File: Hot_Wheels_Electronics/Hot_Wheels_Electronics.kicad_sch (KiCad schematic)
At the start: 42 parts, among them J1 motor_output_a, J2 motor_output_b, J3 Conn_01x05_Socket, J4 Conn_01x02_Socket, J5 Conn_01x03_Socket, J6 Conn_01x06_Socket, J7 Conn_01x04_Socket, J8 Conn_01x02_Socket, M1 motor_driver: DRV8833PW, SW1 main_switch, U1 esp32-wemos-d1-mini, U2 ESP32-WROOM-32, U3 BMI160, U4 MiniBuck_3A, U5 MiniBuck_3A, U6 ADS1115IDGS

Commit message: separate motor connectors from battery family
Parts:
- J1, J2: footprint Connector_JST:JST_PH_S2B-PH-K_1x02_P2.00mm_Horizontal -> Connector_Molex:Molex_Micro-Fit_3.0_43650-0210_1x02-1MP_P3.00mm_Horizontal
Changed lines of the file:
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@@
 			)
 		)
-		(property "Footprint" "Connector_JST:JST_PH_S2B-PH-K_1x02_P2.00mm_Horizontal"
+		(property "Footprint" "Connector_Molex:Molex_Micro-Fit_3.0_43650-0210_1x02-1MP_P3.00mm_Horizontal"
 			(at 160.02 212.09 0)
 			(hide yes)
@@
 			)
 		)
-		(property "Footprint" "Connector_JST:JST_PH_S2B-PH-K_1x02_P2.00mm_Horizontal"
+		(property "Footprint" "Connector_Molex:Molex_Micro-Fit_3.0_43650-0210_1x02-1MP_P3.00mm_Horizontal"
 			(at 158.75 204.47 0)
 			(hide yes)

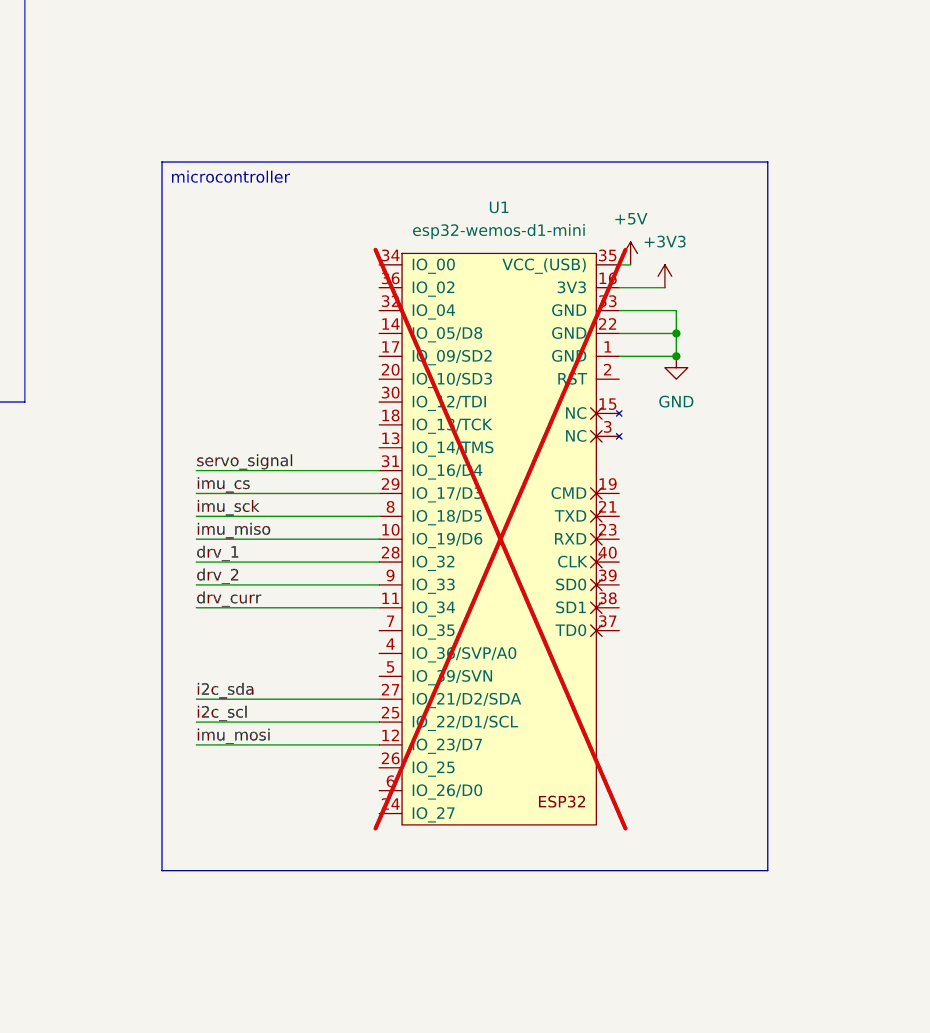
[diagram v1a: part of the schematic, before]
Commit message: archive legacy D1 Mini schematic outside Rev A
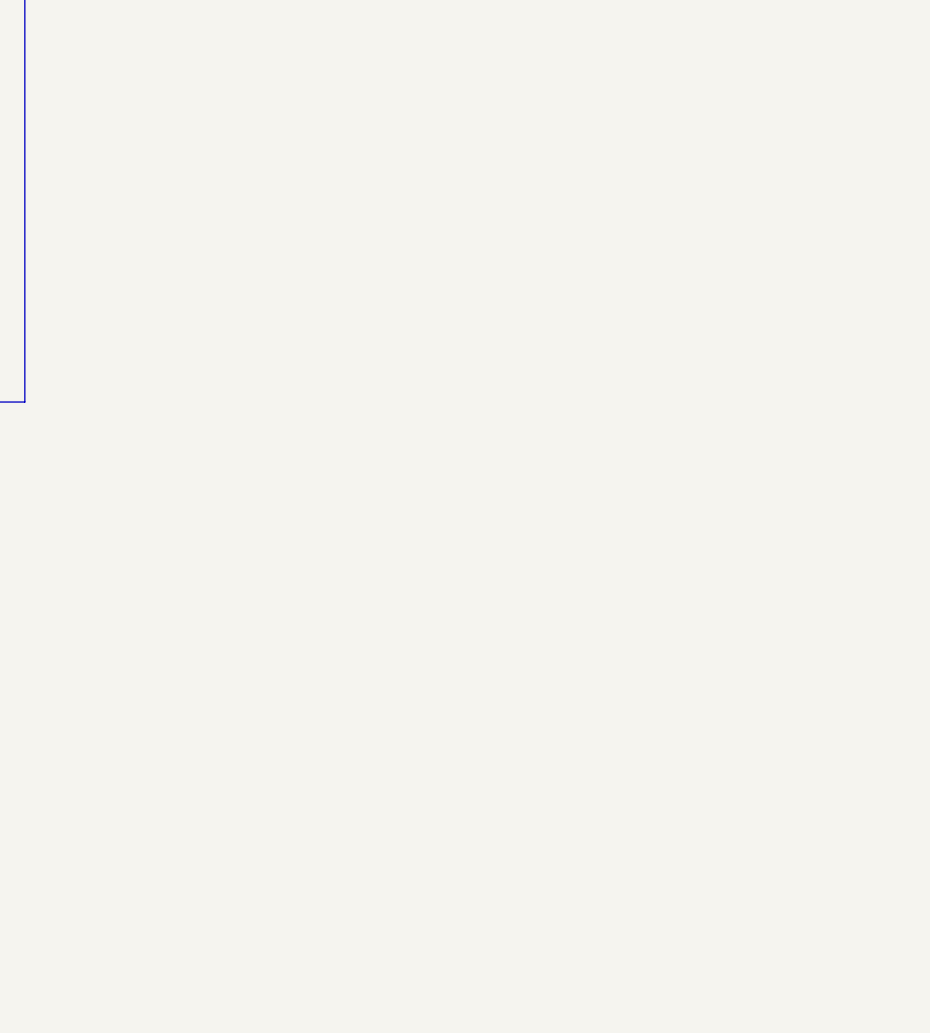
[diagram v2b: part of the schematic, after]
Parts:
- removed U1: esp32-wemos-d1-mini, ESP32_Wemos_D1_Mini_SMD_Socket:ESP32_Wemos_D1_Mini_SMD_Socket_2x20_2.54mm, symbol esp32-wemos-d1-mini:esp32-wemos-d1-mini

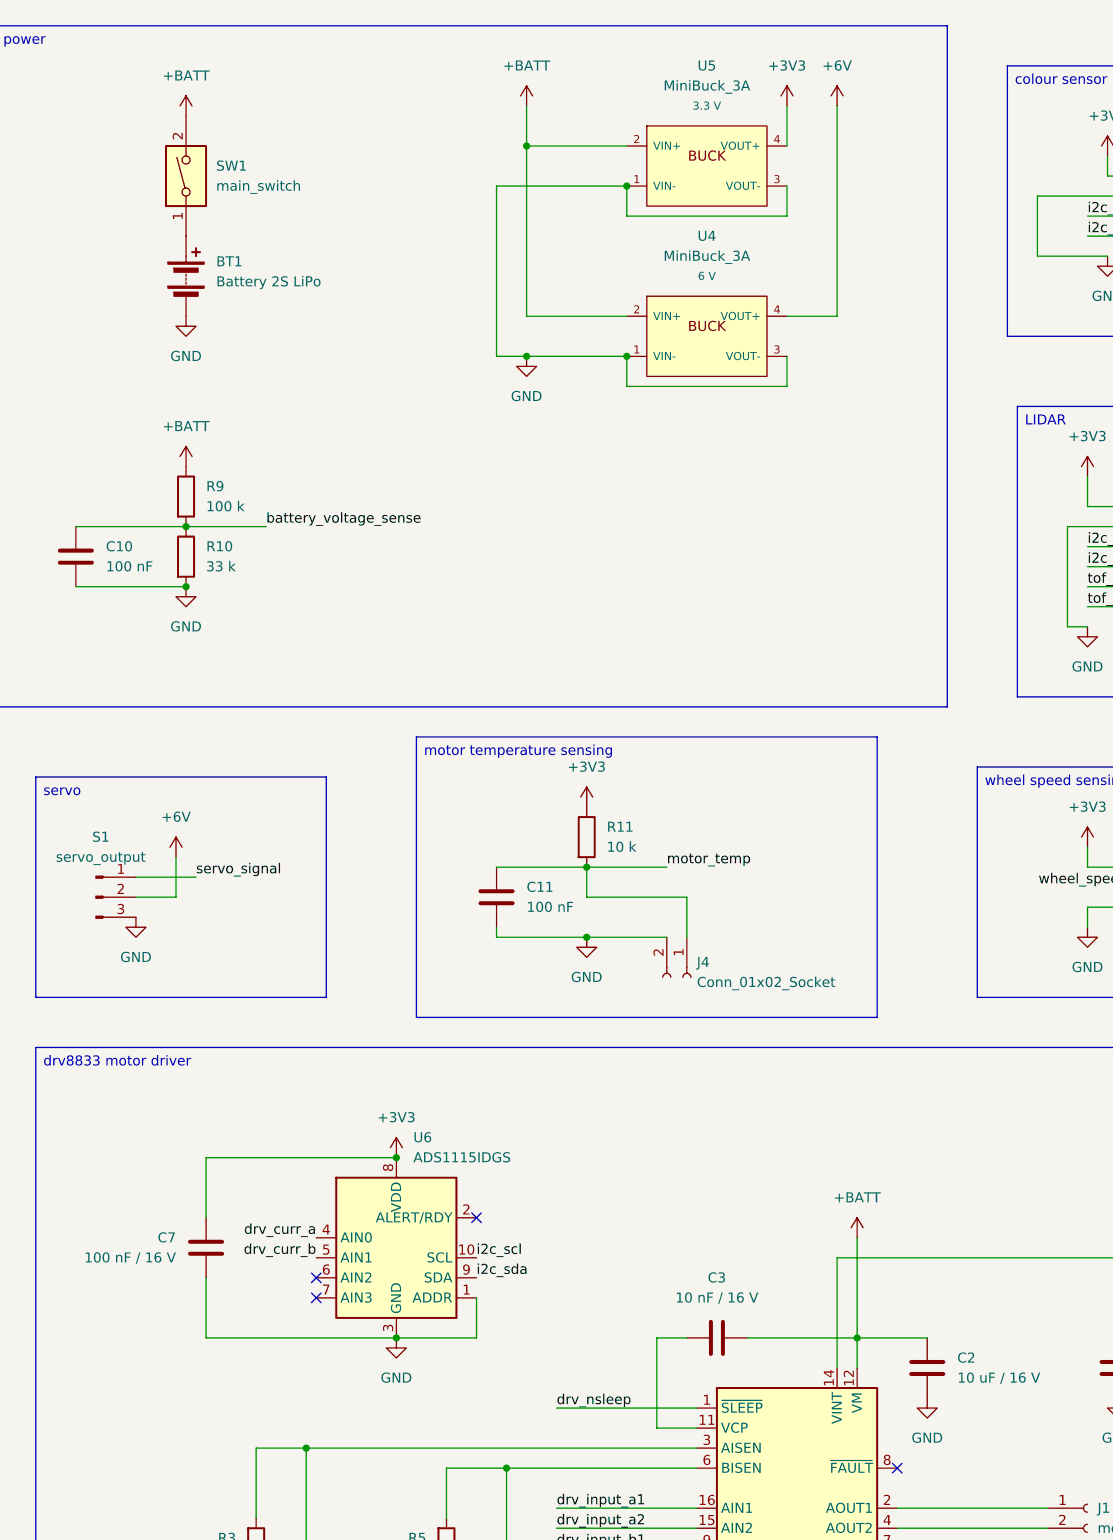
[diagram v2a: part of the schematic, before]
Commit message: model input power and DRV8833 VINT correctly
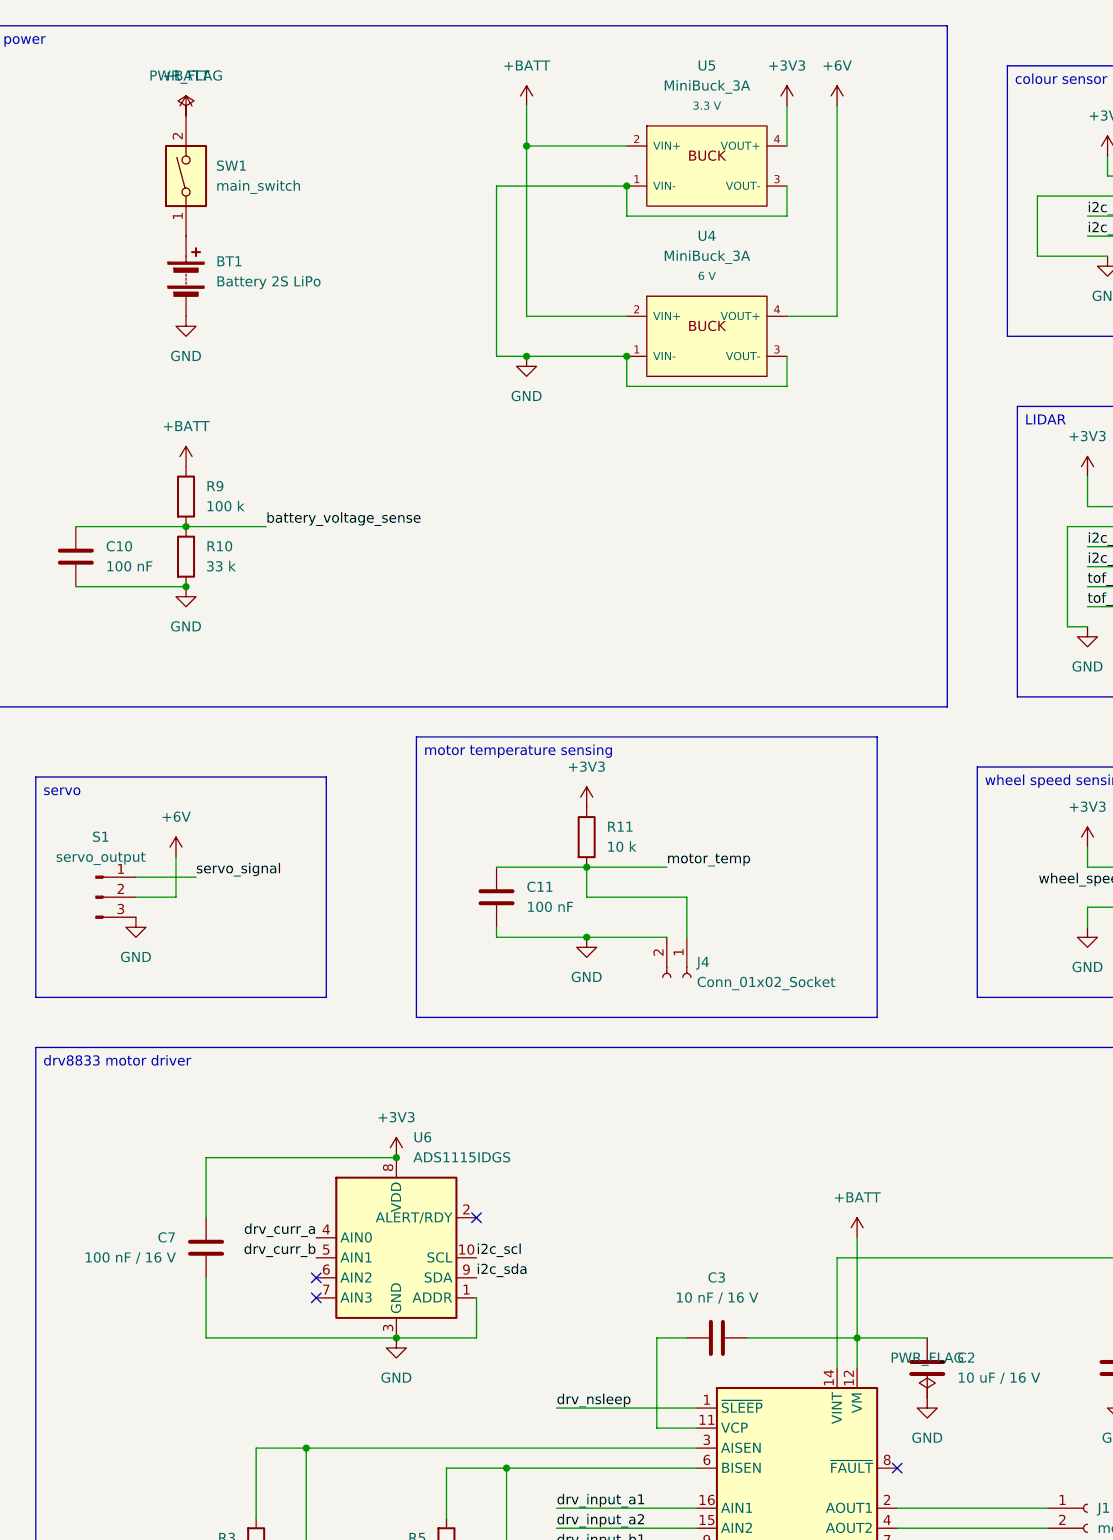
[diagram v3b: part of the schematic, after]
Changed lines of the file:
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@@
+		)
+	)
+	(symbol
+		(lib_id "power:PWR_FLAG")
+		(at 44.4500 27.9400 0)
+		(unit 1)
+		(body_style 1)
+		(exclude_from_sim no)
+		(in_bom yes)
+		(on_board yes)
+		(in_pos_files yes)
+		(dnp no)
+		(fields_autoplaced yes)
+		(property "Reference" "#FLG01"
+			(at 44.4500 31.7500 0)
+			(hide yes)
+			(show_name no)
+			(do_not_autoplace no)
+			(effects
+				(font
+					(size 1.27 1.27)
+				)
+			)
+		)
+		(property "Value" "PWR_FLAG"
+			(at 44.4500 22.8600 0)
+			(show_name no)
+			(do_not_autoplace no)
+			(effects
+				(font
+					(size 1.27 1.27)
+				)
+			)
+		)
+		(property "Footprint" ""
+			(at 44.4500 27.9400 0)
+			(hide yes)
+			(show_name no)
+			(do_not_autoplace no)
+			(effects
+				(font
+					(size 1.27 1.27)
+				)
+			)
+		)
+		(property "Datasheet" ""
+			(at 44.4500 27.9400 0)
+			(hide yes)
+			(show_name no)
+			(do_not_autoplace no)
+			(effects
+				(font
+					(size 1.27 1.27)
+				)
+			)
+		)
+		(property "Description" "Power symbol creates a global label with name \"+3V3\""
+			(at 44.4500 27.9400 0)
+			(hide yes)
+			(show_name no)
+			(do_not_autoplace no)
+			(effects
+				(font
+					(size 1.27 1.27)
+				)
+			)
+		)
+		(pin "1"
+		)
+		(instances
+			(project "Hot_Wheels_Electronics"
+				(path "/753fef37-370a-4893-8adb-358cd7fc1669"
+					(reference "#FLG01")
+					(unit 1)
+				)
+			)
+		)
+	)
+	(symbol
+		(lib_id "power:PWR_FLAG")
+		(at 138.4300 190.5000 0)
+		(unit 1)
+		(body_style 1)
+		(exclude_from_sim no)
+		(in_bom yes)
+		(on_board yes)
+		(in_pos_files yes)
+		(dnp no)
+		(fields_autoplaced yes)
+		(property "Reference" "#FLG02"
+			(at 138.4300 194.3100 0)
+			(hide yes)
+			(show_name no)
+			(do_not_autoplace no)
+			(effects
+				(font
+					(size 1.27 1.27)
+				)
+			)
+		)
+		(property "Value" "PWR_FLAG"
+			(at 138.4300 185.4200 0)
+			(show_name no)
+			(do_not_autoplace no)
+			(effects
+				(font
+					(size 1.27 1.27)
+				)
+			)
+		)
+		(property "Footprint" ""
+			(at 138.4300 190.5000 0)
+			(hide yes)
+			(show_name no)
+			(do_not_autoplace no)
+			(effects
+				(font
+					(size 1.27 1.27)
+				)
+			)
+		)
+		(property "Datasheet" ""
+			(at 138.4300 190.5000 0)
+			(hide yes)
+			(show_name no)
+			(do_not_autoplace no)
+			(effects
+				(font
+					(size 1.27 1.27)
+				)
+			)
+		)
+		(property "Description" "Power symbol creates a global label with name \"+3V3\""
+			(at 138.4300 190.5000 0)
+			(hide yes)
+			(show_name no)
+			(do_not_autoplace no)
+			(effects
+				(font
+					(size 1.27 1.27)
+				)
+			)
+		)
+		(pin "1"
+		)
+		(instances
+			(project "Hot_Wheels_Electronics"
+				(path "/753fef37-370a-4893-8adb-358cd7fc1669"
+					(reference "#FLG02")
+					(unit 1)
+				)
+			)
 		)
 	)

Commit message: add servo rail local decoupling
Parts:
- added C14: 22 uF / 16 V, Capacitor_SMD:C_1210_3225Metric_Pad1.33x2.70mm_HandSolder, symbol Device:C
- added C15: 100 nF / 16 V, Capacitor_SMD:C_1206_3216Metric_Pad1.33x1.80mm_HandSolder, symbol Device:C
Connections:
- net +6V: now also C14.1, C15.1
- net GND: now also C14.2, C15.2

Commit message: add 3.3V WS2812 V6 underglow chain
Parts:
- added D1, D2: WS2812B-2020-V6, LED_SMD:LED_WS2812B-2020_PLCC4_2.0x2.0mm, symbol LED:WS2812B-2020
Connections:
- net +3V3: now also D1.4 (VDD), D2.4 (VDD)
- net GND: now also D1.2 (VSS), D2.2 (VSS)
- net underglow_data: now reaches U2.24 (IO2)
- net underglow_data: now also D1.3 (DIN)
- new net: D1.1 (DOUT), D2.3 (DIN)

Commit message: complete body lighting and audio interfaces
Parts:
- added BZ1: CPT-9019S-SMT-TR, Buzzer_Beeper:Buzzer_CUI_CPT-9019S-SMT, symbol Device:Buzzer
- added J9: body_lights_5p, Connector_JST:JST_ZH_B5B-ZR-SM4-TF_1x05-1MP_P1.50mm_Vertical, symbol Connector:Conn_01x05_Socket
- added Q1, Q2: AO3400A, Package_TO_SOT_SMD:SOT-23, symbol Transistor_FET:Q_NMOS_GSD
- added R16, R17, R18, R19: 470, Resistor_SMD:R_1206_3216Metric_Pad1.30x1.75mm_HandSolder, symbol Device:R
- added R20, R21: 100 k, Resistor_SMD:R_1206_3216Metric_Pad1.30x1.75mm_HandSolder, symbol Device:R
- U2: value ESP32-WROOM-32 -> ESP32-WROOM-32UE-N8
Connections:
- net +3V3: now also U3.12 (CSB)
- net +6V: now also J9.1 (Pin_1)
- net GND: now also U3.1 (SDO), BZ1.2 (-), Q1.2 (S), Q2.2 (S), R20.2, R21.2
- net i2c_scl: now also U3.13 (SCx)
- net i2c_sda: now also U3.14 (SDx)
- net imu_cs renamed light_head_pwm
- net light_head_pwm: now also Q1.1 (G), R20.1; no longer U3.12 (CSB)
- net imu_miso renamed buzzer_pwm
- net buzzer_pwm: now also BZ1.1 (+); no longer U3.1 (SDO)
- net imu_mosi: no longer names the net of U2.37 (IO23)
- net imu_mosi: no longer U3.14 (SDx)
- net imu_sck renamed light_tail_pwm
- net light_tail_pwm: now also Q2.1 (G), R21.1; no longer U3.13 (SCx)
- new net body_head_l: J9.2 (Pin_2), R16.1
- new net body_head_r: J9.3 (Pin_3), R17.1
- new net body_tail_l: J9.4 (Pin_4), R18.1
- new net body_tail_r: J9.5 (Pin_5), R19.1
- new net head_sink: Q1.3 (D), R16.2, R17.2
- new net tail_sink: Q2.3 (D), R18.2, R19.2
- no-connect marks 13 -> 14

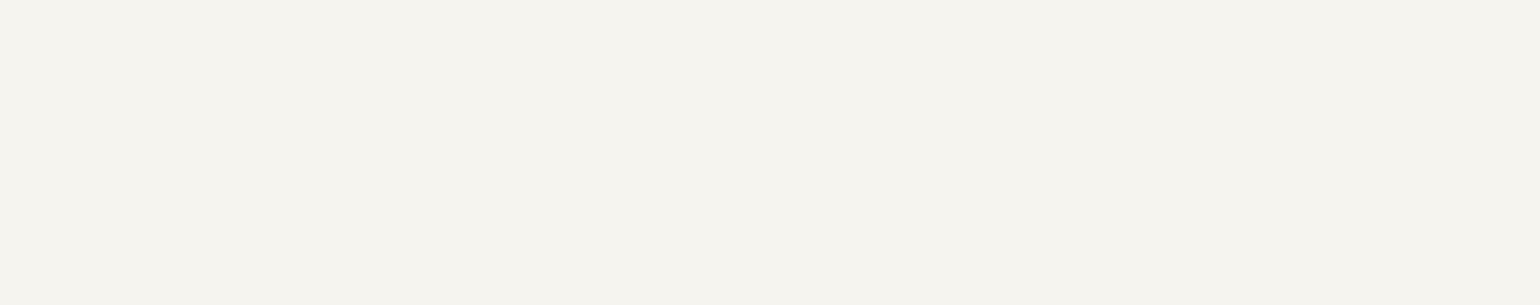
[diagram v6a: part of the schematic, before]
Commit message: add Rev A bring-up test pads
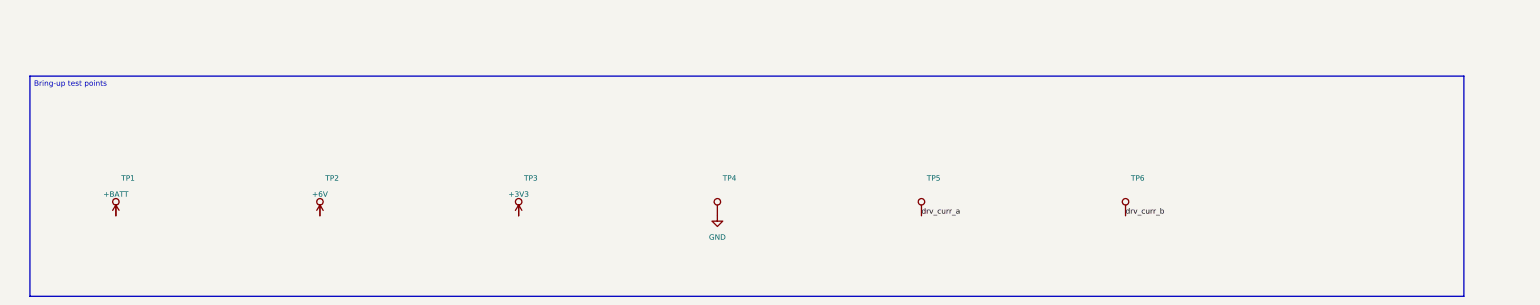
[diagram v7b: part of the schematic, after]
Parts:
- added TP1, TP2, TP3, TP4, TP5, TP6: TestPoint, TestPoint:TestPoint_Pad_D1.5mm, symbol Connector:TestPoint
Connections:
- net +3V3: now also TP3.1
- net +6V: now also TP2.1
- net +BATT: now also TP1.1
- net GND: now also TP4.1
- net drv_curr_a: now also TP5.1
- net drv_curr_b: now also TP6.1
